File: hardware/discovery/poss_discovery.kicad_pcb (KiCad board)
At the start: 2 copper layers, 96.5 x 66 mm, 118 parts, among them CON1 USB-MICRO-B, SW1 SW_PUSH, SW10 SW_PUSH, SW11 SW_PUSH, SW12 SW_PUSH, SW13 SW_PUSH, SW14 SW_PUSH, SW15 SW_PUSH, SW16 SW_PUSH, SW18 SW_PUSH, SW19 SW_PUSH, SW2 SW_PUSH, SW20 SW_PUSH, SW21 SW_PUSH, SW22 SW_PUSH, SW3 SW_PUSH, SW4 SW_PUSH, SW5 SW_PUSH, SW6 SW_PUSH, SW7 SW_PUSH, SW8 SW_PUSH, SW9 SW_PUSH, U10 STM32_SWD_Connector, U2 MCP73831, U3 BD33IA5, U4 STM32F407VG, U5 SGTL5000, U6 encoder_and_switch, U7 encoder_and_switch, U8 MOLEX_microSD_47219-2001, U9 SSD1306, X1 8Mhz

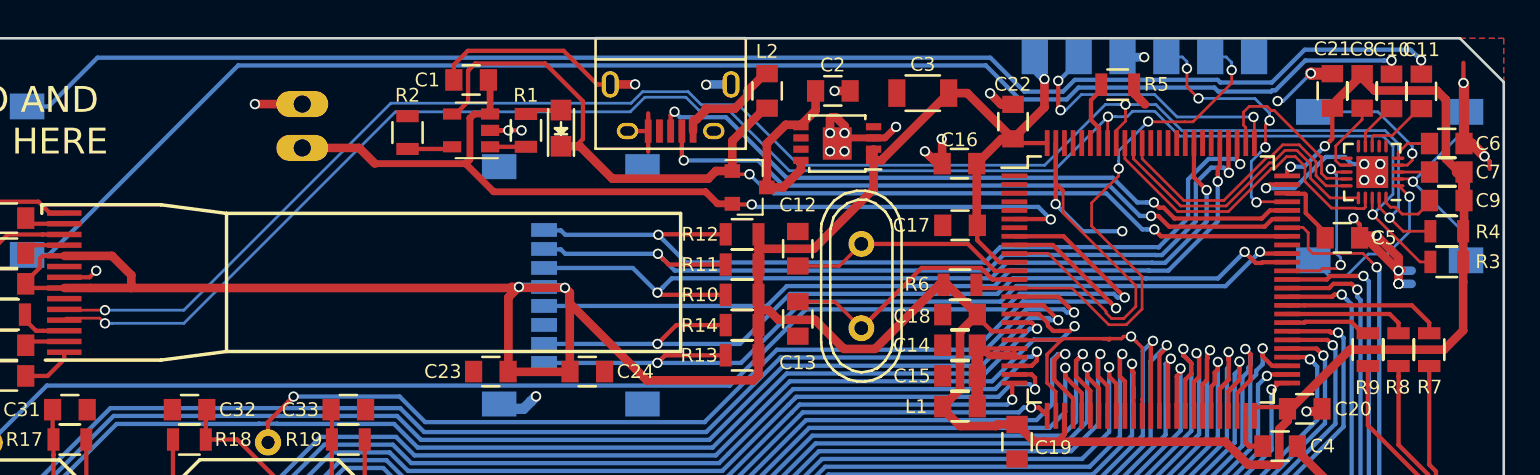
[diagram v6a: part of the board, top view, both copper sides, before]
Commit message: Discovery: A couple of iimprovements in layout
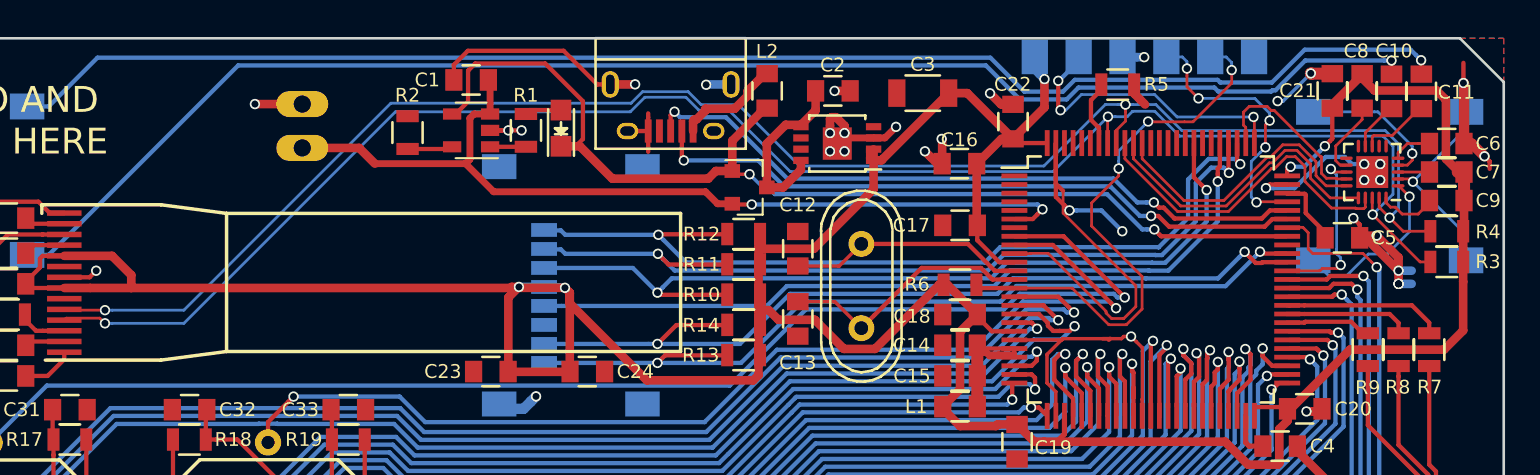
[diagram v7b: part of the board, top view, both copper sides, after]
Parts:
- X1: value 8Mhz -> CRYSTAL
- moved R10 0.09 mm to (132.5, 93.6)
- moved R11 0.09 mm to (132.5, 91.8)
- moved R13 0.09 mm to (132.5, 97.1)
- moved R14 0.09 mm to (132.5, 95.3)
- moved R12 0.09 mm to (132.5, 90.1)
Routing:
- net VBAT: track 53.4 -> 52.4 mm

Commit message: Discovery: Restart from RevA
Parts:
- removed BAT1: LED, LEDs:LED_0805
- removed BT1: BATTERY, Connect:PINHEAD1-2
- removed C1, C25, C26, C27: 10uF, Capacitors_SMD:C_0805
- removed C10, C11, C14, C28, C29: 1uF, Capacitors_SMD:C_0805
- removed C12, C13: C, Capacitors_SMD:C_0805
- removed C15, C17, C18, C19, C20, C21, C22, C23, C6, C7, C8, C9: 0.1uF, Capacitors_SMD:C_0805
- removed C16, C24: 22uF, Capacitors_SMD:C_0805
- removed C2: 4.7uF, Capacitors_SMD:C_0805
- removed C3: 47uF, Capacitors_SMD:C_1206
- removed C30, C31, C32, C33: 0,1uF, Capacitors_SMD:C_0805
- removed C4, C5: 2.2uF, Capacitors_SMD:C_0805
- removed CON1: USB-MICRO-B, Connect:USB_Micro-B
- removed D27: DOUBLE_SCH_KCOM_PMEG2005CT, TO_SOT_Packages_SMD:SOT-23
- removed HP_OUT1, LINE_IN1: 3.5_audio_jack, stm32f4-disco:lumberg_3.5_audio_jack_1503_02
- removed L1, L2: 15Ohm, Capacitors_SMD:C_0805
- removed R1: 1K, Resistors_SMD:R_0805
- removed R10, R11, R12, R13, R14, R2, R3, R4, R5, R6: 10K, Resistors_SMD:R_0805
- removed R15, R7, R8, R9: R, Resistors_SMD:R_0805
- removed R16, R17, R18, R19: 27K, Resistors_SMD:R_0805
- removed U10: STM32_SWD_Connector, stm32f4-disco:STM32_SWD_Connector_SMD
- removed U2: MCP73831, TO_SOT_Packages_SMD:SOT-23-5
- removed U3: BD33IA5, Housings_SSOP:MSOP-8-1EP_3x3mm_Pitch0.65mm
- removed U4: STM32F407VG, Housings_QFP:LQFP-100_14x14mm_Pitch0.5mm
- removed U5: SGTL5000, Housings_DFN_QFN:UQFN-20-1EP_3x3mm_Pitch0.4mm
- removed U6, U7: encoder_and_switch, stm32f4-disco:encoder_EC12D
- removed U8: MOLEX_microSD_47219-2001, stm32f4-disco:MOLEX_microSD_47219-2001
- removed U9: SSD1306, stm32f4-disco:MIDAS_MCOT096016AV_OLED
- removed X1: CRYSTAL, Crystals:Crystal_HC49-U_Vertical
- added D19: LED, LEDs:LED_0805, F.Cu at (97.8, 110.5)
- added J1: HEADER_2, Pin_Headers:Pin_Header_Straight_2x01, F.Cu at (82.5, 85.1)
- added J2: HEADER_25x2, Pin_Headers:Pin_Header_Straight_2x25, F.Cu at (174.0, 85.1)
- added J3: HEADER_25x2, Pin_Headers:Pin_Header_Straight_2x25, F.Cu at (174.0, 135.9)
- added J5: HEADER_2, Pin_Headers:Pin_Header_Straight_2x01, F.Cu at (82.5, 138.4)
- added RV1: POT, Potentiometers:Potentiometer_WirePads_Small, F.Cu at (95.2, 106.4)
- added RV2: POT, Potentiometers:Potentiometer_WirePads_Small, F.Cu at (85.3, 106.4)
- added SW17: SW_PUSH, Buttons_Switches_SMD:SW_SPST_B3SL-1002P, F.Cu at (108.0, 104.1)
- moved D25 82.7 mm to (87.6, 121.9)
- moved D10 81.6 mm to (168.9, 110.5)
- moved D24 62.8 mm to (97.8, 121.9)
- moved D18 61.4 mm to (108.0, 110.5)
- moved D16 44.9 mm to (108.0, 99.1)
- moved D23 43.4 mm to (108.0, 121.9)
- moved D1 41.3 mm to (128.3, 121.9)
- moved D17 41.3 mm to (118.1, 110.5)
- moved D2 41.3 mm to (138.4, 121.9)
- moved D3 41.3 mm to (148.6, 121.9)
- moved D4 41.3 mm to (158.8, 121.9)
- moved D5 41.3 mm to (168.9, 121.9)
- moved D11 35.9 mm to (128.3, 99.1)
- moved D12 35.9 mm to (138.4, 99.1)
- moved D13 35.9 mm to (148.6, 99.1)
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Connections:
- net WAKEUP renamed /GND
- D1 pad 1: COL1 -> /PC9
- D1 pad 2: Net-(D1-Pad2) -> /COL1
- D10 pad 1: COL1 -> /PA8
- D10 pad 2: Net-(D10-Pad2) -> /COL2
- D11 pad 1: COL2 -> /PC9
- D11 pad 2: Net-(D10-Pad2) -> /COL3
- D12 pad 1: COL3 -> /PC8
- D12 pad 2: Net-(D10-Pad2) -> /COL3
- D13 pad 1: COL4 -> /PA15
- D13 pad 2: Net-(D10-Pad2) -> /COL3
- D14 pad 1: COL5 -> /PC11
- D14 pad 2: Net-(D10-Pad2) -> /COL3
- D15 pad 1: COL6 -> /PA8
- D15 pad 2: Net-(D10-Pad2) -> /COL3
- D16 pad 1: COL7 -> /PC9
- D16 pad 2: Net-(D10-Pad2) -> /COL4
- D17 pad 1: COL8 -> /PC8
- D17 pad 2: Net-(D10-Pad2) -> /COL4
- D18 pad 1: COL9 -> /PA15
- D18 pad 2: Net-(D10-Pad2) -> /COL4
- D2 pad 1: COL2 -> /PC8
- D2 pad 2: Net-(D1-Pad2) -> /COL1
- D20 pad 1: COL4 -> /PA8
- D20 pad 2: Net-(D20-Pad2) -> /COL4
- D21 pad 1: COL5 -> /PC9
- D21 pad 2: Net-(D20-Pad2) -> /COL5
- D22 pad 1: COL6 -> /PC8
- D22 pad 2: Net-(D20-Pad2) -> /COL5
- D23 pad 1: COL7 -> /PA15
- D23 pad 2: Net-(D20-Pad2) -> /COL5
- D24 pad 1: COL8 -> /PC11
- D24 pad 2: Net-(D20-Pad2) -> /COL5
- D25 pad 1: COL9 -> /PA8
- D25 pad 2: Net-(D20-Pad2) -> /COL5
- D3 pad 1: COL3 -> /PA15
- D3 pad 2: Net-(D1-Pad2) -> /COL1
- D4 pad 1: COL4 -> /PC11
- D4 pad 2: Net-(D1-Pad2) -> /COL1
- D5 pad 1: COL5 -> /PA8
- D5 pad 2: Net-(D1-Pad2) -> /COL1
- D6 pad 1: COL6 -> /PC9
- D6 pad 2: Net-(D1-Pad2) -> /COL2
- D7 pad 1: COL7 -> /PC8
- D7 pad 2: Net-(D1-Pad2) -> /COL2
- D8 pad 1: COL8 -> /PA15
- D8 pad 2: Net-(D1-Pad2) -> /COL2
- D9 pad 1: COL9 -> /PC11
- D9 pad 2: Net-(D1-Pad2) -> /COL2
- Play1 pad 1: Play -> /PD0
- Play2 pad 1: FX -> /FX
- SW1 pad 1: B1 -> /B1
- SW10 pad 1: B10 -> /B10
- SW11 pad 1: B11 -> /B11
- SW12 pad 1: B12 -> /B12
- SW13 pad 1: B13 -> /B13
- SW14 pad 1: B14 -> /B14
- SW15 pad 1: B15 -> /B15
- SW16 pad 1: B16 -> /B16
- SW18 pad 1: BA -> /BF2
- SW19 pad 1: BB -> /BF3
- SW2 pad 1: B2 -> /B2
- SW20 pad 1: BC -> /BF4
- SW21 pad 1: BD -> /BF5
- SW22 pad 1: BE -> /BPM
- SW3 pad 1: B3 -> /B3
- SW4 pad 1: B4 -> /B4
- SW5 pad 1: B5 -> /B5
- SW6 pad 1: B6 -> /B6
- SW7 pad 1: B7 -> /B7
- SW8 pad 1: B8 -> /B8
- SW9 pad 1: B9 -> /B9
- Write1 pad 1: Write -> /PD2
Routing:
- net /GND: track 346.7 -> 42.0 mm, vias 1 -> 13
- net 3V3: track 214.2 -> 0.00 mm, vias 5 -> 0
- net /PA8: track 0.00 -> 172.4 mm, vias 0 -> 5
- net /PA15: track 0.00 -> 146.8 mm, vias 0 -> 6
- net /PC11: track 0.00 -> 142.5 mm, vias 0 -> 6
- net /PC8: track 0.00 -> 125.1 mm, vias 0 -> 7
- net Net-(D1-Pad2): track 124.5 -> 0.00 mm, vias 2 -> 0
- net GND: track 120.9 -> 0.00 mm, vias 36 -> 0
- net /PC9: track 0.00 -> 118.0 mm, vias 0 -> 5
- net Net-(D10-Pad2): track 113.4 -> 0.00 mm, vias 2 -> 0
- net B9: track 101.4 -> 0.00 mm, vias 2 -> 0
- net Audio_SDA: track 98.1 -> 0.00 mm, vias 3 -> 0
- net COL1: track 97.8 -> 0.00 mm, vias 3 -> 0
- net Audio_SCL: track 97.8 -> 0.00 mm, vias 3 -> 0
- net COL2: track 95.7 -> 0.00 mm, vias 3 -> 0
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- added copper zone on B.Cu, net /GND
- added copper zone on F.Cu, net /GND
- removed copper zone on B.Cu, net GND
- removed copper zone on F.Cu, net GND
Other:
- net class DAC_traces removed
- net class power removed
- rule trace_min: 0.16 -> 0.2
- board text added: "BPM"
- board text removed: "GND"
- board text removed: "IN"
- board text removed: "LOGO AND NAME HERE"
- board text removed: "NRST"
- board text removed: "OUT"
- board text removed: "RevB"
- board text removed: "SWCLK"
- board text removed: "SWDIO"
- board text removed: "SWO"
- board text removed: "VCC"
